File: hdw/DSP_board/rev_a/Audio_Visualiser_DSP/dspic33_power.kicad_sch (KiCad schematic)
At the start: 20 parts

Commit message: lots of early schematic progress
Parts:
- added C?: 1000pF, symbol Custom Library:C_Custom
- L?: footprint (none) -> Inductors_SMD:L_0805; Ampacity A -> 0.56A; Digi-Key PN (none) -> 118-SRN2012T-100KCT-ND; Tolerance Tol -> 10%; display_footprint Foot -> 0805
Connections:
- net +3.3VA_DSP: now also C?.1
- net GNDA_DSP: now also C?.2
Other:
- moved on the sheet: C?

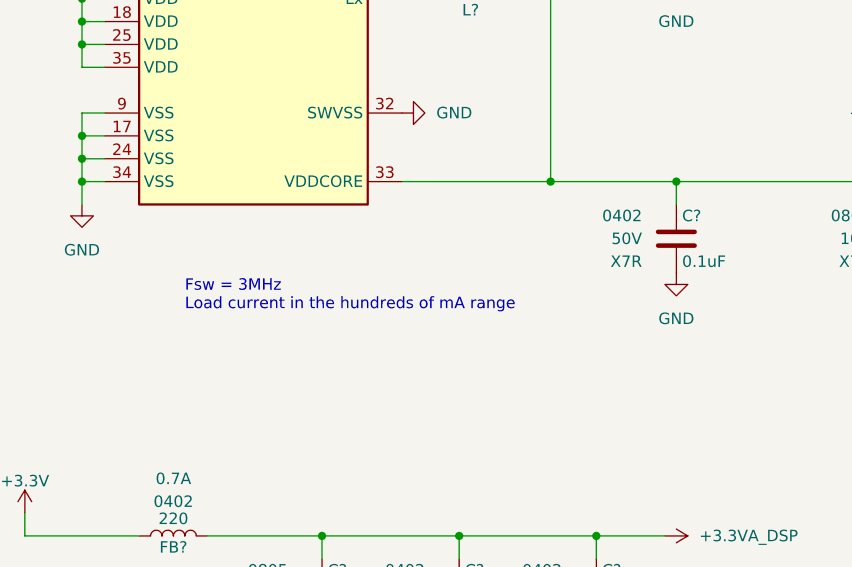
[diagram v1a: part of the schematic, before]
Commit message: added a ton of circuitry in schematic, new USB UART bridge, other random stuff
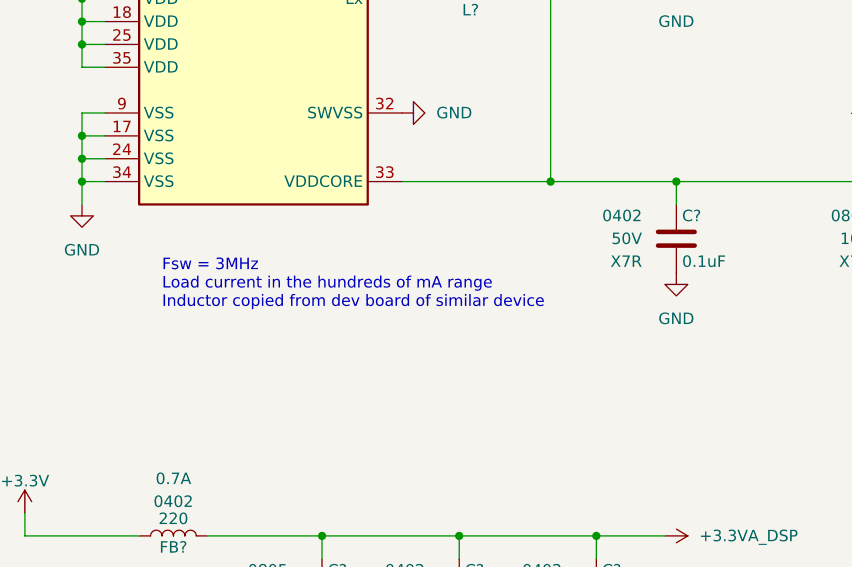
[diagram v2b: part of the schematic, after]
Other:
- note added: "Fsw = 3MHz Load current in the hundreds of mA range Inductor copied from dev board of similar device"
- note removed: "Fsw = 3MHz Load current in the hundreds of mA range"

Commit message: Changed to 48 pin dsPIC
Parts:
- removed U?: dsPIC33AK256MPS103, Package_DFN_QFN:QFN-36-1EP_5x5mm_P0.4mm_EP3.7x3.7mm, symbol dsPIC33AK256MPS103:dsPIC33AK256MPS103
- added U?: dsPIC33AK256MPS105, Package_DFN_QFN:QFN-48-1EP_6x6mm_P0.4mm_EP4.1x4.1mm, symbol dsPIC33AK256MPS105:dsPIC33AK256MPS105
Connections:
- net +1.2V_VCORE: now also U?.44 (VDDCORE)
- net +3.3V: now also U?.15 (VDD), U?.28 (VDD), U?.36 (VDD), U?.41 (SWVDD), U?.46 (VDD)
- net +3.3VA_DSP: now also U?.7 (AVDD)
- net GND: now also U?.14 (VSS), U?.27 (VSS), U?.35 (VSS), U?.43 (SWVSS), U?.45 (VSS)
- net GNDA_DSP: now also U?.6 (AVSS)
- net ~{DSPIC33_MCLR}: now also U?.48 (~{MCLR})
- net at L?.1: now also U?.42 (Lx)
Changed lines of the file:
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@@
+	)
+	(symbol
+		(lib_id "dsPIC33AK256MPS105:dsPIC33AK256MPS105")
+		(at 157.48 77.47 0)
+		(unit 1)
+		(body_style 1)
+		(exclude_from_sim no)
+		(in_bom yes)
+		(on_board yes)
+		(in_pos_files yes)
+		(dnp no)
+		(fields_autoplaced yes)
+		(property "Reference" "U?"
+			(at 157.48 46.99 0)
+			(show_name no)
+			(do_not_autoplace no)
+			(effects
+				(font
+					(size 1.27 1.27)
+				)
+			)
+		)
+		(property "Value" "dsPIC33AK256MPS105"
+			(at 157.48 49.53 0)
+			(show_name no)
+			(do_not_autoplace no)
+			(effects
+				(font
+					(size 1.27 1.27)
+				)
+			)
+		)
+		(property "Footprint" "Package_DFN_QFN:QFN-48-1EP_6x6mm_P0.4mm_EP4.1x4.1mm"
+			(at 137.16 52.07 0)
+			(hide yes)
+			(show_name no)
+			(do_not_autoplace no)
+			(effects
+				(font
+					(size 1.27 1.27)
+				)
+				(justify left)
+			)
+		)
+		(property "Datasheet" "https://ww1.microchip.com/downloads/aemDocuments/documents/MCU16/ProductDocuments/DataSheets/dsPIC33AK256MPS306-Family-Data-Sheet-DS70005629.pdf"
+			(at 137.16 54.61 0)
+			(hide yes)
+			(show_name no)
+			(do_not_autoplace no)
+			(effects
+				(font
+					(size 1.27 1.27)
+				)
+				(justify left)
+			)
+		)
+		(property "Description" "200 MHz 32-bit dsPIC33A Digital Signal Controller (DSC), FPU, High-Res PWM, High-Speed ADC, 256KB Flash, 64KB SRAM, 48-Pin VQFN/TQFP, no CAN FD"
+			(at 157.48 77.47 0)
+			(hide yes)
+			(show_name no)
+			(do_not_autoplace no)
+			(effects
+				(font
+					(size 1.27 1.27)
+				)
+				(justify left)
+			)
+		)
+		(property "Keywords" "dsPIC33A DSC digital signal controller microcontroller motor control FOC"
+			(at 157.48 77.47 0)
+			(hide yes)
+			(show_name no)
+			(do_not_autoplace no)
+			(effects
+				(font
+					(size 1.27 1.27)
+				)
+				(justify left)
+			)
+		)
+		(property "Digi-Key PN" "DSPIC33AK256MPS105-I/M7"
+			(at 157.48 77.47 0)
+			(hide yes)
+			(show_name no)
+			(do_not_autoplace no)
+			(effects
+				(font
+					(size 1.27 1.27)
+				)
+				(justify left)
+			)
+		)
+		(pin "17"
+		)
+		(pin "4"
+		)
+		(pin "27"
+		)
+		(pin "15"
+		)
+		(pin "46"
+		)
+		(pin "35"
+		)
+		(pin "48"
+		)
+		(pin "47"
+		)
+		(pin "21"
+		)
+		(pin "24"
+		)
+		(pin "37"
+		)
+		(pin "2"
+		)
+		(pin "22"
+		)
+		(pin "1"
+		)
+		(pin "41"
+		)
+		(pin "16"
+		)
+		(pin "23"
+		)
+		(pin "33"
+		)
+		(pin "40"
+		)
+		(pin "13"
+		)
+		(pin "14"
+		)
+		(pin "12"
+		)
+		(pin "19"
+		)
+		(pin "20"
+		)
+		(pin "28"
+		)
+		(pin "44"
+		)
+		(pin "5"
+		)
+		(pin "18"
+		)
+		(pin "38"
+		)
+		(pin "31"
+		)
+		(pin "3"
+		)
+		(pin "8"
+		)
+		(pin "42"
+		)
+		(pin "45"
+		)
+		(pin "10"
+		)
+		(pin "6"
+		)
+		(pin "36"
+		)
+		(pin "25"
+		)
+		(pin "11"
+		)
+		(pin "43"
+		)
+		(pin "29"
+		)
+		(pin "30"
+		)
+		(pin "32"
+		)
+		(pin "34"
+		)
+		(pin "7"
+		)
+		(pin "9"
+		)
+		(pin "26"
+		)
+		(pin "39"
+		)
+		(instances
+			(project "Audio_Visualiser_DSP"
+				(path "/97a4dfb8-0e16-46f1-9709-8d2007dd0cd3/0e59d275-c36c-4218-b5cc-8096e466612c"
+					(reference "U?")
+					(unit 1)
+				)
+			)
+		)
 	)
 	(symbol
@@
 					(unit 1)
 				)
-			)
-		)
-	)
-	(symbol
-		(lib_id "dsPIC33AK256MPS103:dsPIC33AK256MPS103")
-		(at 157.48 77.47 0)
-		(unit 1)
-		(body_style 1)
-		(exclude_from_sim no)
-		(in_bom yes)
-		(on_board yes)
-		(in_pos_files yes)
-		(dnp no)
-		(fields_autoplaced yes)
-		(property "Reference" "U?"
-			(at 157.48 46.99 0)
-			(show_name no)
-			(do_not_autoplace no)
-			(effects
-				(font
-					(size 1.27 1.27)
-				)
-			)
-		)
-		(property "Value" "dsPIC33AK256MPS103"
-			(at 157.48 49.53 0)
-			(show_name no)
-			(do_not_autoplace no)
-			(effects
-				(font
-					(size 1.27 1.27)
-				)
-			)
-		)
-		(property "Footprint" "Package_DFN_QFN:QFN-36-1EP_5x5mm_P0.4mm_EP3.7x3.7mm"
-			(at 137.16 52.07 0)
-			(hide yes)
-			(show_name no)
-			(do_not_autoplace no)
-			(effects
-				(font
-					(size 1.27 1.27)
-				)
-				(justify left)
-			)
-		)
-		(property "Datasheet" "https://ww1.microchip.com/downloads/aemDocuments/documents/MCU16/ProductDocuments/DataSheets/dsPIC33AK256MPS306-Family-Data-Sheet-DS70005629.pdf"
-			(at 137.16 54.61 0)
-			(hide yes)
-			(show_name no)
-			(do_not_autoplace no)
-			(effects
-				(font
-					(size 1.27 1.27)
-				)
-				(justify left)
-			)
-		)
-		(property "Description" "200 MHz 32-bit dsPIC33A Digital Signal Controller (DSC), FPU, High-Res PWM, High-Speed ADC, 256KB Flash, 64KB SRAM, 36-Pin VQFN, no CAN FD"
-			(at 157.48 77.47 0)
-			(hide yes)
-			(show_name no)
-			(do_not_autoplace no)
-			(effects
-				(font
-					(size 1.27 1.27)
-				)
-				(justify left)
-			)
-		)
-		(property "Keywords" "dsPIC33A DSC digital signal controller microcontroller motor control FOC"
-			(at 157.48 77.47 0)
-			(hide yes)
-			(show_name no)
-			(do_not_autoplace no)
-			(effects
-				(font
-					(size 1.27 1.27)
-				)
-				(justify left)
-			)
-		)
-		(property "Digi-Key PN" "DSPIC33AK256MPS103-I/M7"
-			(at 157.48 77.47 0)
-			(hide yes)
-			(show_name no)
-			(do_not_autoplace no)
-			(effects
-				(font
-					(size 1.27 1.27)
-				)
-				(justify left)
-			)
-		)
-		(pin "28"
-		)
-		(pin "27"
-		)
-		(pin "19"
-		)
-		(pin "12"
-		)
-		(pin "5"
-		)
-		(pin "1"
-		)
-		(pin "14"
-		)
-		(pin "10"
-		)
-		(pin "20"
-		)
-		(pin "17"
-		)
-		(pin "18"
-		)
-		(pin "4"
-		)
-		(pin "32"
-		)
-		(pin "24"
-		)
-		(pin "34"
-		)
-		(pin "35"
-		)
-		(pin "2"
-		)
-		(pin "9"
-		)
-		(pin "3"
-		)
-		(pin "7"
-		)
-		(pin "8"
-		)
-		(pin "13"
-		)
-		(pin "15"
-		)
-		(pin "16"
-		)
-		(pin "11"
-		)
-		(pin "23"
-		)
-		(pin "21"
-		)
-		(pin "26"
-		)
-		(pin "36"
-		)
-		(pin "33"
-		)
-		(pin "25"
-		)
-		(pin "31"
-		)
-		(pin "30"
-		)
-		(pin "6"
-		)
-		(pin "22"
-		)
-		(pin "29"
-		)
-		(instances
-			(project "Audio_Visualiser_DSP"
-				(path "/97a4dfb8-0e16-46f1-9709-8d2007dd0cd3/0e59d275-c36c-4218-b5cc-8096e466612c"
-					(reference "U?")
-					(unit 1)
-				)

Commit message: Added some spice models
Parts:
- gave numbers to parts that had none: 21

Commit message: added rotary encoder circuitry
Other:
- note added: "Two 10uF edge caps"
- note removed: "Two 10uF edge cap"
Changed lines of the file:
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@@
 		)
 	)
-	(text "Two 10uF edge cap"
+	(text "Two 10uF edge caps"
 		(exclude_from_sim no)
 		(at 31.75 166.37 0)

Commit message: Annotated schematic
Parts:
- renumbered C20 to C701, C21 to C702, C22 to C703, C23 to C704, C24 to C705, C25 to C706, C26 to C707, C27 to C708, C28 to C709, C29 to C710, C30 to C711, C31 to C712, C32 to C713, C33 to C714, C34 to C715, C35 to C716, C36 to C717, FB4 to FB701, FB5 to FB702, L2 to L701, U7 to U701

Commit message: cleared stale digikey part numbers
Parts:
- C701, C702, C703, C704, C706, C707, C708, C709, C712, C713, C714, C715: footprint (none) -> Capacitors_SMD:C_0402; Digi-Key PN PN -> (none)
- C705, C710, C711, C716, C717: footprint (none) -> Capacitors_SMD:C_0805; Digi-Key PN PN -> (none)
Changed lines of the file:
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@@
 			)
 		)
-		(property "Footprint" ""
+		(property "Footprint" "Capacitors_SMD:C_0402"
 			(at 64.4652 86.36 0)
 			(hide yes)
@@
 			)
 		)
-		(property "Digi-Key PN" "PN"
+		(property "Digi-Key PN" ""
 			(at 74.295 69.85 0)
 			(hide yes)
@@
 			)
 		)
-		(property "Footprint" ""
+		(property "Footprint" "Capacitors_SMD:C_0805"
 			(at 166.0652 154.94 0)
 			(hide yes)
@@
 			)
 		)
-		(property "Digi-Key PN" "PN"
+		(property "Digi-Key PN" ""
 			(at 175.895 138.43 0)
 			(hide yes)
@@
 			)
 		)
-		(property "Footprint" ""
+		(property "Footprint" "Capacitors_SMD:C_0402"
 			(at 181.3052 154.94 0)
 			(hide yes)
@@
 			)
 		)
-		(property "Digi-Key PN" "PN"
+		(property "Digi-Key PN" ""
 			(at 191.135 138.43 0)
 			(hide yes)
@@
 			)
 		)
-		(property "Footprint" ""
+		(property "Footprint" "Capacitors_SMD:C_0402"
 			(at 64.4652 60.96 0)
 			(hide yes)
@@
 			)
 		)
-		(property "Digi-Key PN" "PN"
+		(property "Digi-Key PN" ""
 			(at 74.295 44.45 0)
 			(hide yes)
@@
 			)
 		)
-		(property "Footprint" ""
+		(property "Footprint" "Capacitors_SMD:C_0805"
 			(at 64.4652 171.45 0)
 			(hide yes)
@@
 			)
 		)
-		(property "Digi-Key PN" "PN"
+		(property "Digi-Key PN" ""
 			(at 74.295 154.94 0)
 			(hide yes)
@@
 			)
 		)
-		(property "Footprint" ""
+		(property "Footprint" "Capacitors_SMD:C_0402"
 			(at 205.4352 82.55 0)
 			(hide yes)
@@
 			)
 		)
-		(property "Digi-Key PN" "PN"
+		(property "Digi-Key PN" ""
 			(at 215.265 66.04 0)
 			(hide yes)
@@
 			)
 		)
-		(property "Footprint" ""
+		(property "Footprint" "Capacitors_SMD:C_0805"
 			(at 230.8352 115.57 0)
 			(hide yes)
@@
 			)
 		)
-		(property "Digi-Key PN" "PN"
+		(property "Digi-Key PN" ""
 			(at 240.665 99.06 0)
 			(hide yes)
@@
 			)
 		)
-		(property "Footprint" ""
+		(property "Footprint" "Capacitors_SMD:C_0402"
 			(at 89.8652 60.96 0)
 			(hide yes)
@@
 			)
 		)
-		(property "Digi-Key PN" "PN"
+		(property "Digi-Key PN" ""
 			(at 99.695 44.45 0)
 			(hide yes)
@@
 			)
 		)
-		(property "Footprint" ""
+		(property "Footprint" "Capacitors_SMD:C_0805"
 			(at 89.8652 171.45 0)
 			(hide yes)
@@
 			)
 		)
-		(property "Digi-Key PN" "PN"
+		(property "Digi-Key PN" ""
 			(at 99.695 154.94 0)
 			(hide yes)
@@
 			)
 		)
-		(property "Footprint" ""
+		(property "Footprint" "Capacitors_SMD:C_0402"
 			(at 64.4652 137.16 0)
 			(hide yes)
@@
 			)
 		)
-		(property "Digi-Key PN" "PN"
+		(property "Digi-Key PN" ""
 			(at 74.295 120.65 0)
 			(hide yes)
@@
 			)
 		)
-		(property "Footprint" ""
+		(property "Footprint" "Capacitors_SMD:C_0805"
 			(at 230.8352 82.55 0)
 			(hide yes)
@@
 			)
 		)
-		(property "Digi-Key PN" "PN"
+		(property "Digi-Key PN" ""
 			(at 240.665 66.04 0)
 			(hide yes)
@@
 			)
 		)
-		(property "Footprint" ""
+		(property "Footprint" "Capacitors_SMD:C_0402"
 			(at 196.5452 154.94 0)
 			(hide yes)
@@
 			)
 		)
-		(property "Digi-Key PN" "PN"
+		(property "Digi-Key PN" ""
 			(at 206.375 138.43 0)
 			(hide yes)
@@
 			)
 		)
-		(property "Footprint" ""
+		(property "Footprint" "Capacitors_SMD:C_0402"
 			(at 89.8652 137.16 0)
 			(hide yes)
@@
 			)
 		)
-		(property "Digi-Key PN" "PN"
+		(property "Digi-Key PN" ""
 			(at 99.695 120.65 0)
 			(hide yes)
@@
 			)
 		)
-		(property "Footprint" ""
+		(property "Footprint" "Capacitors_SMD:C_0402"
 			(at 205.4352 115.57 0)
 			(hide yes)
@@
 			)
 		)
-		(property "Digi-Key PN" "PN"
+		(property "Digi-Key PN" ""
 			(at 215.265 99.06 0)
 			(hide yes)
@@
 			)
 		)
-		(property "Footprint" ""
+		(property "Footprint" "Capacitors_SMD:C_0402"
 			(at 64.4652 111.76 0)
 			(hide yes)
@@
 			)
 		)
-		(property "Digi-Key PN" "PN"
+		(property "Digi-Key PN" ""
 			(at 74.295 95.25 0)
 			(hide yes)
@@
 			)
 		)
-		(property "Footprint" ""
+		(property "Footprint" "Capacitors_SMD:C_0402"
 			(at 89.8652 86.36 0)
 			(hide yes)
@@
 			)
 		)
-		(property "Digi-Key PN" "PN"
+		(property "Digi-Key PN" ""
 			(at 99.695 69.85 0)
 			(hide yes)
@@
 			)
 		)
-		(property "Footprint" ""
+		(property "Footprint" "Capacitors_SMD:C_0402"
 			(at 89.8652 111.76 0)
 			(hide yes)
@@
 			)
 		)
-		(property "Digi-Key PN" "PN"
+		(property "Digi-Key PN" ""
 			(at 99.695 95.25 0)
 			(hide yes)
